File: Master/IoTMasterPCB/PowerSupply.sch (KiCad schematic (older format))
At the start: 0 parts

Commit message: Work on Master Board schematics; added full Zigbee. Added RFID module. Added USB/power supply, as well as MCU decoupling.
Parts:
- added C?: 4.7 µF, Capacitor_SMD:C_0805_2012Metric, symbol Device:C
- added C?: 10 µF, Capacitor_SMD:C_0805_2012Metric, symbol Device:C
- added D?: 5.6 V, Diode_SMD:D_MiniMELF, symbol Device:D_Zener_Small
- added FB?: 120 @ 100 MHz, Inductor_SMD:L_0603_1608Metric, symbol Device:Ferrite_Bead_Small
- added FL?: ECMF02-4CMX8, Personal_Passives:ECMF024CMX8, symbol Personal_Passives:ECMF02-4CMX8
- added J?: 10118194-0001LF, Personal_Misc:10118194-0001LF, symbol Personal_Misc:10118194-0001LF
- added R?: 0R, Resistor_SMD:R_1206_3216Metric, symbol Device:R
- added U?: MYRGP330100B21RA, Personal_ICs:MYRGP180100B21RA, symbol Personal_ICs:MYRGP330100B21RA
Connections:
- new net: U?.1 (LX), U?.7 (L1)
- new net: FB?.2, J?.1 (VBUS)
- new net: FL?.2 (D-_I), J?.2 (D-)
- new net: FL?.3 (D+_I), J?.3 (D+)
- new net +3V3: C?.2, U?.3 (VOUT), U?.8 (L2)
- new net +5V: C?.2, D?.1 (K), FB?.1, FL?.1 (VBUS), U?.4 (CE), U?.6 (VIN)
- new net GND: C?.1, C?.1, D?.2 (A), FL?.5 (GND), FL?.8 (GND), J?.5 (GND), R?.1, U?.2 (AGND), U?.5 (PGND), U?.9 (EP)
- new net GND1: J?.S1 (Shield), R?.2
- new net USB_N: FL?.7 (D-_O)
- new net USB_P: FL?.6 (D+_O)
- no-connect marks 0 -> 2
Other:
- note added: "3 A"
- note added: "3.3 V converter"
- note added: "USB circuit"
- note added: "~~90% efficiency above 10 mA."

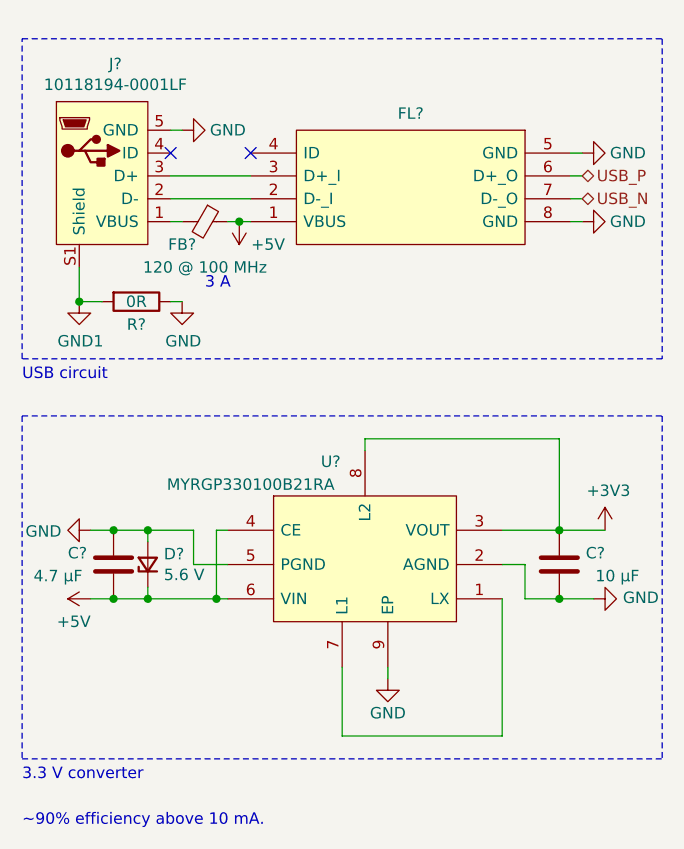
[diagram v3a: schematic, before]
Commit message: Finished RFID module sans antenna footprint. Added KSZ8081MNX and hierarchial connections.
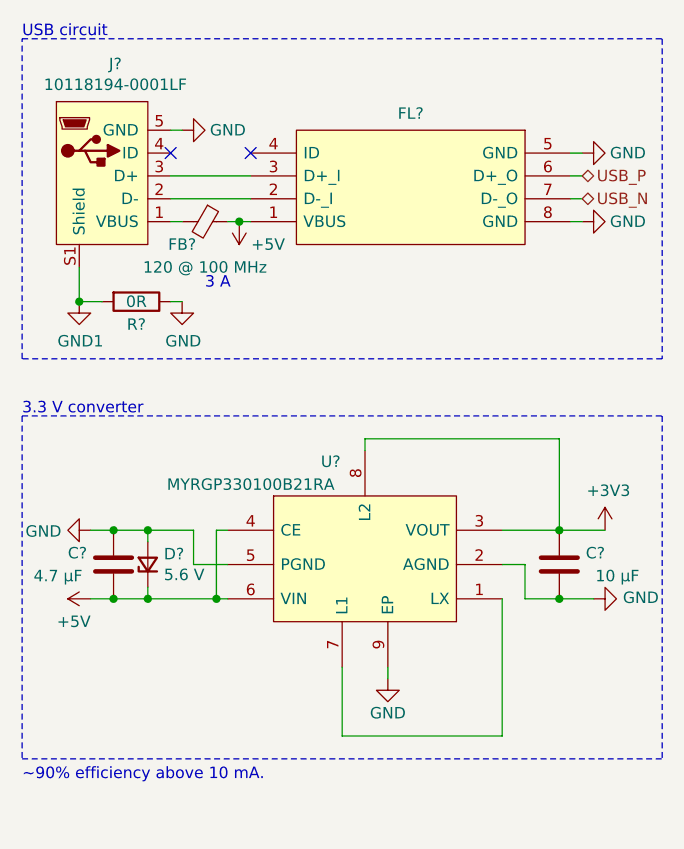
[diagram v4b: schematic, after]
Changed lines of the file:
@@
 Wire Notes Line
 	3850 2350 1050 2350
-Text Notes 1050 2450 0    50   ~ 0
+Text Notes 1050 950  0    50   ~ 0
 USB circuit
 $Comp
@@
 Wire Notes Line
 	1050 2600 1050 4100
+Text Notes 1050 2600 0    50   ~ 0
+3.3 V converter
 Text Notes 1050 4200 0    50   ~ 0
-3.3 V converter
-Text Notes 1050 4400 0    50   ~ 0
 ~~90% efficiency above 10 mA.
 Wire Notes Line

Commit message: Finished RFID and Ethernet circuits.
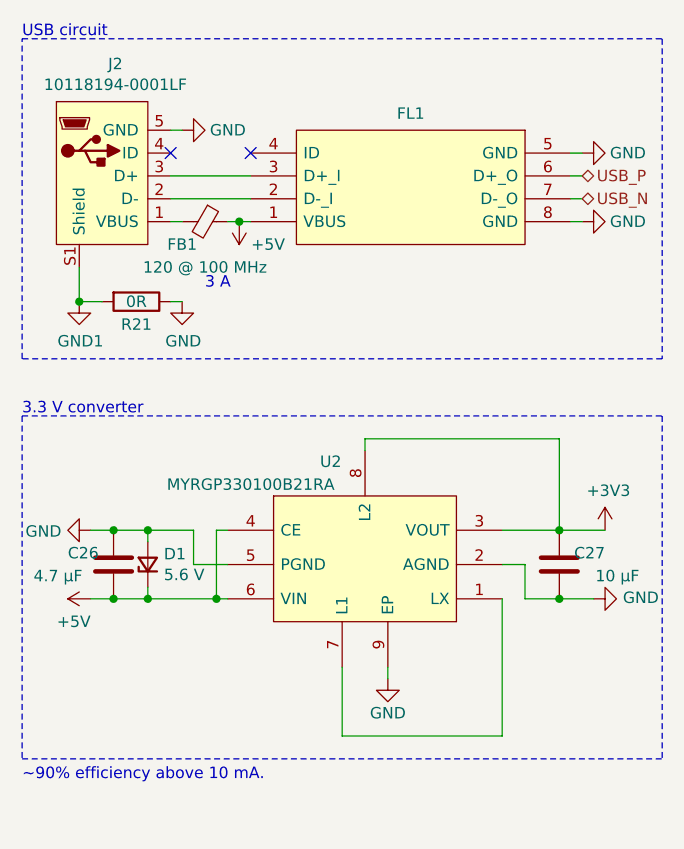
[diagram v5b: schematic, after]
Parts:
- gave numbers to parts that had none: 8
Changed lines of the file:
@@
 $EndDescr
 $Comp
-L Personal_Misc:10118194-0001LF J?
+L Personal_Misc:10118194-0001LF J2
 U 1 1 60025E4F
 P 1700 1350
-F 0 "J?" H 1458 1640 50  0000 C CNN
+F 0 "J2" H 1458 1640 50  0000 C CNN
 F 1 "10118194-0001LF" H 1458 1549 50  0000 C CNN
 F 2 "Personal_Misc:10118194-0001LF" H 2150 1425 50  0001 L BNN
@@
 NoConn ~ 1700 1450
 $Comp
-L power:GND1 #PWR?
+L power:GND1 #PWR0114
 U 1 1 60025E56
 P 1300 2100
-F 0 "#PWR?" H 1300 1850 50  0001 C CNN
+F 0 "#PWR0114" H 1300 1850 50  0001 C CNN
 F 1 "GND1" H 1305 1927 50  0000 C CNN
 F 2 "" H 1300 2100 50  0001 C CNN
@@
 Connection ~ 1300 2100
 $Comp
-L Device:R R?
+L Device:R R21
 U 1 1 60025E5E
 P 1550 2100
-F 0 "R?" V 1650 2100 50  0000 C CNN
+F 0 "R21" V 1650 2100 50  0000 C CNN
 F 1 "0R" V 1550 2100 50  0000 C CNN
 F 2 "Resistor_SMD:R_1206_3216Metric" V 1480 2100 50  0001 C CNN
@@
 	1700 2100 1750 2100
 $Comp
-L power:GND #PWR?
+L power:GND #PWR0115
 U 1 1 60025E65
 P 1750 2100
-F 0 "#PWR?" H 1750 1850 50  0001 C CNN
+F 0 "#PWR0115" H 1750 1850 50  0001 C CNN
 F 1 "GND" H 1755 1927 50  0000 C CNN
 F 2 "" H 1750 2100 50  0001 C CNN
@@
 $EndComp
 $Comp
-L power:GND #PWR?
+L power:GND #PWR0116
 U 1 1 60025E6B
 P 1750 1350
-F 0 "#PWR?" H 1750 1100 50  0001 C CNN
+F 0 "#PWR0116" H 1750 1100 50  0001 C CNN
 F 1 "GND" V 1750 1150 50  0000 C CNN
 F 2 "" H 1750 1350 50  0001 C CNN
@@
 	1750 1750 1700 1750
 $Comp
-L power:+5V #PWR?
+L power:+5V #PWR0117
 U 1 1 60025E73
 P 2000 1750
-F 0 "#PWR?" H 2000 1600 50  0001 C CNN
+F 0 "#PWR0117" H 2000 1600 50  0001 C CNN
 F 1 "+5V" H 1800 1850 50  0000 L CNN
 F 2 "" H 2000 1750 50  0001 C CNN
@@
 P 1850 1750
 AR Path="/5F9F06B0/60025E79" Ref="FB?"  Part="1"
-AR Path="/5F9EEC7C/60025E79" Ref="FB?"  Part="1"
-F 0 "FB?" V 1950 1650 50  0000 C CNN
+AR Path="/5F9EEC7C/60025E79" Ref="FB1"  Part="1"
+F 0 "FB1" V 1950 1650 50  0000 C CNN
 F 1 "120 @ 100 MHz" V 2050 1750 50  0000 C CNN
 F 2 "Inductor_SMD:L_0603_1608Metric" V 1780 1750 50  0001 C CNN
@@
 3 A
 $Comp
-L Personal_Passives:ECMF02-4CMX8 FL?
+L Personal_Passives:ECMF02-4CMX8 FL1
 U 1 1 60025E88
 P 2050 1450
-F 0 "FL?" H 2750 1623 50  0000 C CNN
+F 0 "FL1" H 2750 1623 50  0000 C CNN
 F 1 "ECMF02-4CMX8" H 2100 1800 50  0001 L CNN
 F 2 "Personal_Passives:ECMF024CMX8" H 2100 2200 50  0001 L CNN
@@
 NoConn ~ 2050 1450
 $Comp
-L power:GND #PWR?
+L power:GND #PWR0118
 U 1 1 60025E91
 P 3500 1450
-F 0 "#PWR?" H 3500 1200 50  0001 C CNN
+F 0 "#PWR0118" H 3500 1200 50  0001 C CNN
 F 1 "GND" V 3500 1250 50  0000 C CNN
 F 2 "" H 3500 1450 50  0001 C CNN
@@
 	3500 1450 3450 1450
 $Comp
-L power:GND #PWR?
+L power:GND #PWR0119
 U 1 1 60025E98
 P 3500 1750
-F 0 "#PWR?" H 3500 1500 50  0001 C CNN
+F 0 "#PWR0119" H 3500 1500 50  0001 C CNN
 F 1 "GND" V 3500 1550 50  0000 C CNN
 F 2 "" H 3500 1750 50  0001 C CNN
@@
 USB circuit
 $Comp
-L Personal_ICs:MYRGP330100B21RA U?
+L Personal_ICs:MYRGP330100B21RA U2
 U 1 1 5FCB71D2
 P 1950 3100
-F 0 "U?" H 2400 3400 50  0000 C CNN
+F 0 "U2" H 2400 3400 50  0000 C CNN
 F 1 "MYRGP330100B21RA" H 2050 3300 50  0000 C CNN
 F 2 "Personal_ICs:MYRGP180100B21RA" H 2700 3300 50  0001 L CNN
@@
 $EndComp
 $Comp
-L power:GND #PWR?
+L power:GND #PWR0120
 U 1 1 5FCBC1C7
 P 2650 3750
-F 0 "#PWR?" H 2650 3500 50  0001 C CNN
+F 0 "#PWR0120" H 2650 3500 50  0001 C CNN
 F 1 "GND" H 2650 3600 50  0000 C CNN
 F 2 "" H 2650 3750 50  0001 C CNN
@@
 	2650 3700 2650 3750
 $Comp
-L power:GND #PWR?
+L power:GND #PWR0121
 U 1 1 5FCBC1CE
 P 1350 3100
-F 0 "#PWR?" H 1350 2850 50  0001 C CNN
+F 0 "#PWR0121" H 1350 2850 50  0001 C CNN
 F 1 "GND" V 1355 2972 50  0000 R CNN
 F 2 "" H 1350 3100 50  0001 C CNN
@@
 $EndComp
 $Comp
-L Device:C C?
+L Device:C C26
 U 1 1 5FCBC1DA
 P 1450 3250
-F 0 "C?" H 1250 3300 50  0000 L CNN
+F 0 "C26" H 1250 3300 50  0000 L CNN
 F 1 "4.7 µF" H 1100 3200 50  0000 L CNN
 F 2 "Capacitor_SMD:C_0805_2012Metric" H 1488 3100 50  0001 C CNN
@@
 	1350 3400 1450 3400
 $Comp
-L power:GND #PWR?
+L power:GND #PWR0122
 U 1 1 5FCBC1E4
 P 3550 3400
-F 0 "#PWR?" H 3550 3150 50  0001 C CNN
+F 0 "#PWR0122" H 3550 3150 50  0001 C CNN
 F 1 "GND" V 3555 3272 50  0000 R CNN
 F 2 "" H 3550 3400 50  0001 C CNN
@@
 $EndComp
 $Comp
-L Device:C C?
+L Device:C C27
 U 1 1 5FCBC1EA
 P 3400 3250
-F 0 "C?" H 3200 3200 50  0000 L CNN
+F 0 "C27" H 3200 3200 50  0000 L CNN
 F 1 "10 µF" H 3050 3300 50  0000 L CNN
 F 2 "Capacitor_SMD:C_0805_2012Metric" H 3438 3100 50  0001 C CNN
@@
 	1050 4100 3850 4100
 $Comp
-L power:+3V3 #PWR?
+L power:+3V3 #PWR0123
 U 1 1 5FCC3DB7
 P 3600 3100
-F 0 "#PWR?" H 3600 2950 50  0001 C CNN
+F 0 "#PWR0123" H 3600 2950 50  0001 C CNN
 F 1 "+3V3" H 3615 3273 50  0000 C CNN
 F 2 "" H 3600 3100 50  0001 C CNN
@@
 $EndComp
 $Comp
-L power:+5V #PWR?
+L power:+5V #PWR0124
 U 1 1 5FCC488C
 P 1350 3400
-F 0 "#PWR?" H 1350 3250 50  0001 C CNN
+F 0 "#PWR0124" H 1350 3250 50  0001 C CNN
 F 1 "+5V" V 1250 3400 50  0000 L CNN
 F 2 "" H 1350 3400 50  0001 C CNN
@@
 $EndComp
 $Comp
-L Device:D_Zener_Small D?
+L Device:D_Zener_Small D1
 U 1 1 5FCF858A
 P 1600 3250
-F 0 "D?" V 1646 3180 50  0000 R CNN
+F 0 "D1" V 1646 3180 50  0000 R CNN
 F 1 "5.6 V" V 1555 3180 50  0000 R CNN
 F 2 "Diode_SMD:D_MiniMELF" V 1600 3250 50  0001 C CNN
